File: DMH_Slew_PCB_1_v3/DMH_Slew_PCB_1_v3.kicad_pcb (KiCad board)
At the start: 2 copper layers, 48 x 175 mm, 33 parts, among them J0 Conn_01x01, J1 TS_Jack_6.35mm_Sw, J10 TS_Jack_6.35mm_Sw, J100 IDC_02x08, J14 Conn_02x03_Top_Bottom, J15 Conn_02x06_Top_Bottom, J16 Conn_02x03_Top_Bottom, J17 Conn_01x08, J18 Conn_01x08, J2 TS_Jack_6.35mm_Sw, J200 IDC_02x05, J24 Conn_02x03_Top_Bottom, J25 Conn_02x06_Top_Bottom, J26 Conn_02x03_Top_Bottom, J27 Conn_01x08, J28 Conn_01x08, J3 TS_Jack_6.35mm_Sw, J4 TS_Jack_6.35mm_Sw, J5 TS_Jack_6.35mm_Sw, J6 TS_Jack_6.35mm_Sw, J7 TS_Jack_6.35mm_Sw, J8 TS_Jack_6.35mm_Sw, J9 TS_Jack_6.35mm_Sw, U10 LM4040LP-10, U11 LM4040LP-10

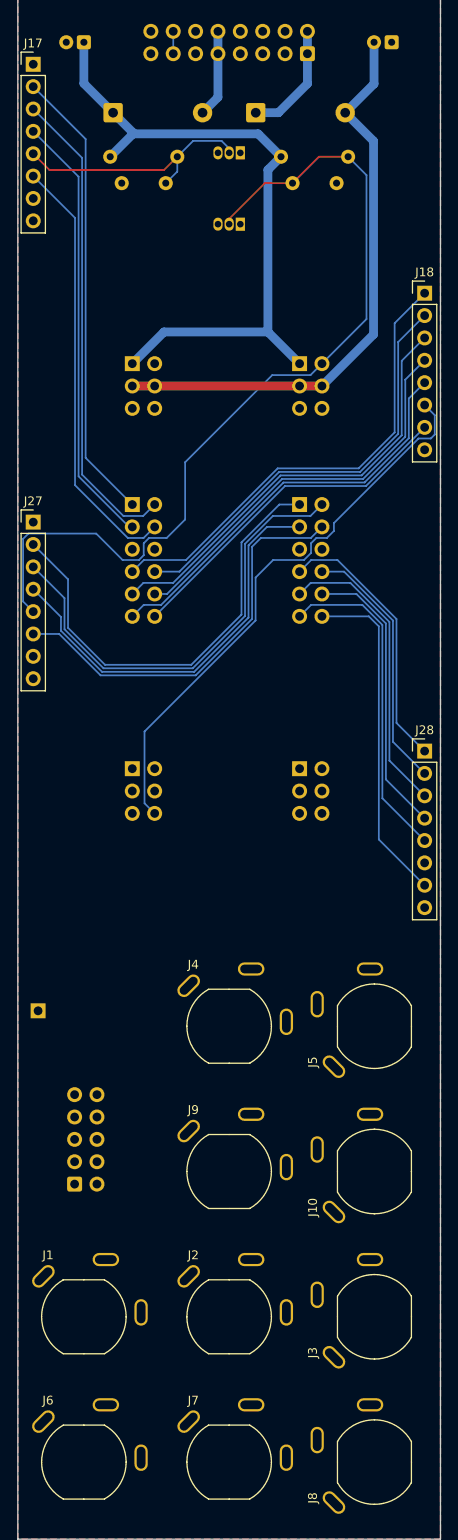
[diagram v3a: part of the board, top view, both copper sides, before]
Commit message: PCB 1 Routing done
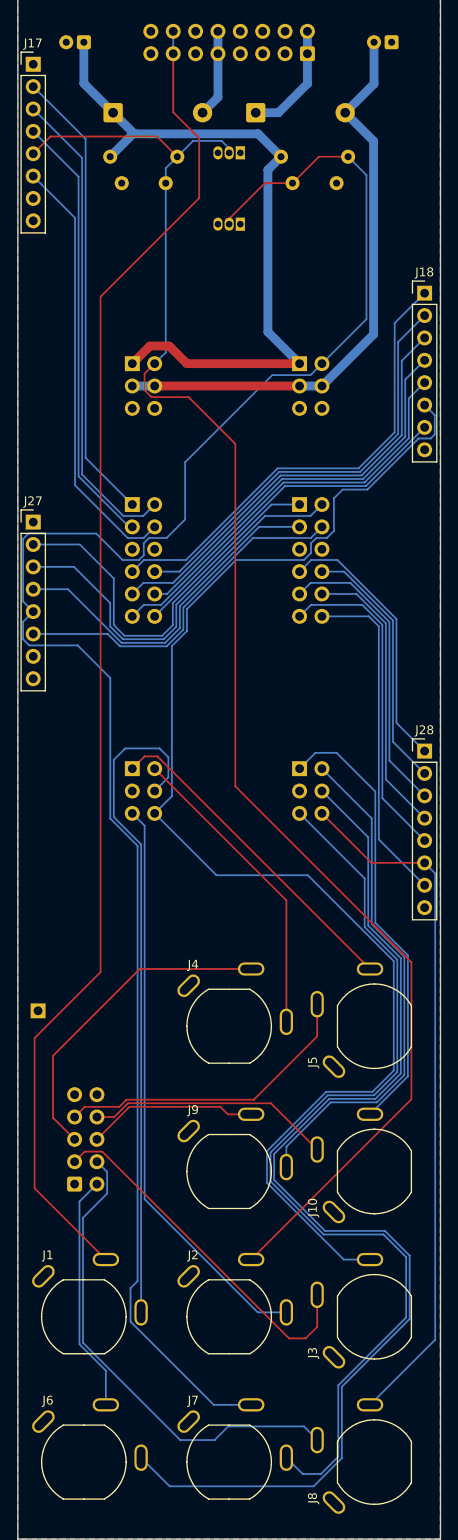
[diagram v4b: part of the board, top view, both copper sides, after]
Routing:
- net Bus_CV_M: track 2.54 -> 151.8 mm
- net +10V_A: track 28.8 -> 175.0 mm
- net B_Input_Jack_M: track 0.00 -> 127.5 mm
- net B_CV_In_Jack_M: track 0.00 -> 107.7 mm
- net +10V_B: track 101.5 -> 209.2 mm
- net A_Out_Jack_M: track 64.6 -> 151.3 mm
- net B_Out_Jack_M: track 0.00 -> 79.1 mm
- net A_Input_Jack_M: track 0.00 -> 75.7 mm
- net A_CV_In_Jack_M: track 0.00 -> 65.8 mm
- net B_R_Gate_Jack_M: track 0.00 -> 57.8 mm
- net B_Out_Jack_TN_M: track 0.00 -> 54.7 mm
- net B_F_Gate_Jack_M: track 0.00 -> 51.1 mm
- net A_Out_Jack_TN_M: track 0.00 -> 41.0 mm
- net A_F_Gate_Jack_M: track 0.00 -> 37.6 mm
- net A_R_Gate_Jack_TN_M: track 0.00 -> 37.1 mm
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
